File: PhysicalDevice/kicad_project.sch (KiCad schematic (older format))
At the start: 22 parts, among them J1 Conn_01x06, SW1 SW_Push, SW2 SW_Push, SW3 SW_Push, U1 MAX7219CWGT, U3 AMS1117-3.3

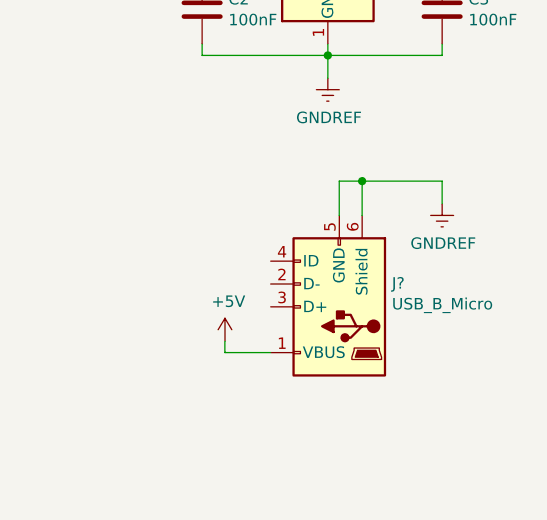
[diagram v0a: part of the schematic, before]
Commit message: Board fully routed. Gerber file generated.
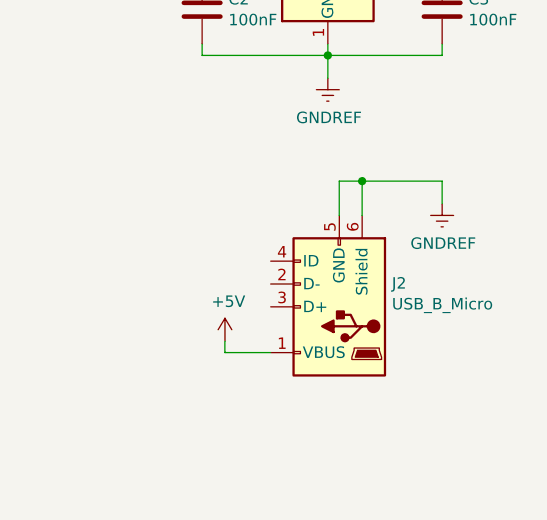
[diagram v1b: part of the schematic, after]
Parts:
- gave numbers to parts that had none: 1
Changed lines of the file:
@@
 BUT_OFFSET
 $Comp
-L Connector:USB_B_Micro J?
+L Connector:USB_B_Micro J2
 U 1 1 5D204B92
 P 9550 5350
-F 0 "J?" H 9320 5247 50  0000 R CNN
+F 0 "J2" H 9320 5247 50  0000 R CNN
 F 1 "USB_B_Micro" H 9320 5338 50  0000 R CNN
 F 2 "Connector_USB:USB_Micro-B_Molex-105017-0001" H 9700 5300 50  0001 C CNN
@@
 $EndComp
 $Comp
-L power:GNDREF #PWR?
+L power:GNDREF #PWR0117
 U 1 1 5D2071A6
 P 10000 4900
-F 0 "#PWR?" H 10000 4650 50  0001 C CNN
+F 0 "#PWR0117" H 10000 4650 50  0001 C CNN
 F 1 "GNDREF" H 10005 4727 50  0000 C CNN
 F 2 "" H 10000 4900 50  0001 C CNN
@@
 	9650 4800 10000 4800
 $Comp
-L power:+5V #PWR?
+L power:+5V #PWR0118
 U 1 1 5D20C16A
 P 9050 5500
-F 0 "#PWR?" H 9050 5350 50  0001 C CNN
+F 0 "#PWR0118" H 9050 5350 50  0001 C CNN
 F 1 "+5V" H 9065 5673 50  0000 C CNN
 F 2 "" H 9050 5500 50  0001 C CNN

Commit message: added leds and rerouted some bits to be more tidy
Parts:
- added CONN1, WPS1: LED, LED_SMD:LED_0805_2012Metric_Pad1.15x1.40mm_HandSolder, symbol Device:LED
- added R8: 220R, Resistor_SMD:R_0805_2012Metric_Pad1.15x1.40mm_HandSolder, symbol Device:R_Small
- added R9: 2204, Resistor_SMD:R_0805_2012Metric_Pad1.15x1.40mm_HandSolder, symbol Device:R_Small
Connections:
- net GNDREF: now also CONN1.1 (K), WPS1.1 (K)
- net LED_CONN: now reaches ESP12E1.17 (GPIO2)
- net LED_CONN: now also R9.2
- net LED_WPS: now reaches ESP12E1.4 (GPIO16)
- net LED_WPS: now also R8.2
- new net: R8.1, WPS1.2 (A)
- new net: CONN1.2 (A), R9.1
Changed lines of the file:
@@
 Wire Wire Line
 	9050 5550 9050 5500
+$Comp
+L Device:R_Small R8
+U 1 1 5D140AC3
+P 6100 5500
+F 0 "R8" H 6159 5546 50  0000 L CNN
+F 1 "220R" H 6159 5455 50  0000 L CNN
+F 2 "Resistor_SMD:R_0805_2012Metric_Pad1.15x1.40mm_HandSolder" H 6100 5500 50  0001 C CNN
+F 3 "~" H 6100 5500 50  0001 C CNN
+	1    6100 5500
+	0    1    1    0
+$EndComp
+$Comp
+L Device:R_Small R9
+U 1 1 5D142792
+P 6100 5900
+F 0 "R9" H 6159 5946 50  0000 L CNN
+F 1 "2204" H 6159 5855 50  0000 L CNN
+F 2 "Resistor_SMD:R_0805_2012Metric_Pad1.15x1.40mm_HandSolder" H 6100 5900 50  0001 C CNN
+F 3 "~" H 6100 5900 50  0001 C CNN
+	1    6100 5900
+	0    1    1    0
+$EndComp
+Wire Wire Line
+	6650 5500 6850 5500
+Wire Wire Line
+	6850 5500 6850 5900
+Wire Wire Line
+	6850 5900 6650 5900
+Wire Wire Line
+	6850 5900 6850 6000
+Connection ~ 6850 5900
+$Comp
+L power:GNDREF #PWR0119
+U 1 1 5D14BF49
+P 6850 6000
+F 0 "#PWR0119" H 6850 5750 50  0001 C CNN
+F 1 "GNDREF" H 6855 5827 50  0000 C CNN
+F 2 "" H 6850 6000 50  0001 C CNN
+F 3 "" H 6850 6000 50  0001 C CNN
+	1    6850 6000
+	1    0    0    -1
+$EndComp
+Text Label 7250 1800 0    50   ~ 0
+LED_CONN
+Text Label 7250 2600 3    50   ~ 0
+LED_WPS
+Text Label 6000 5900 2    50   ~ 0
+LED_CONN
+Text Label 6000 5500 2    50   ~ 0
+LED_WPS
+$Comp
+L Device:LED CONN1
+U 1 1 5D139E9D
+P 6500 5900
+F 0 "CONN1" H 6493 5645 50  0000 C CNN
+F 1 "LED" H 6493 5736 50  0000 C CNN
+F 2 "LED_SMD:LED_0805_2012Metric_Pad1.15x1.40mm_HandSolder" H 6500 5900 50  0001 C CNN
+F 3 "~" H 6500 5900 50  0001 C CNN
+	1    6500 5900
+	-1   0    0    1
+$EndComp
+$Comp
+L Device:LED WPS1
+U 1 1 5D138DE4
+P 6500 5500
+F 0 "WPS1" H 6493 5245 50  0000 C CNN
+F 1 "LED" H 6493 5336 50  0000 C CNN
+F 2 "LED_SMD:LED_0805_2012Metric_Pad1.15x1.40mm_HandSolder" H 6500 5500 50  0001 C CNN
+F 3 "~" H 6500 5500 50  0001 C CNN
+	1    6500 5500
+	-1   0    0    1
+$EndComp
+Wire Wire Line
+	6200 5500 6350 5500
+Wire Wire Line
+	6350 5900 6200 5900
 $EndSCHEMATC

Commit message: pre track witdh change
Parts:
- added SW4: SW_Push, KicadLibrary:DTS-3, symbol Switch:SW_Push
- SW1, SW2, SW3: footprint Button_Switch_THT:SW_PUSH_6mm -> KicadLibrary:DTS-3
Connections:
- net DIG_4 is gone; now on net GNDREF: U1.3 (DIG_4)
- net DIG_5 is gone; now on net GNDREF: U1.10 (DIG_5)
- net DIG_7 is gone; now on net GNDREF: U1.8 (DIG_7)
- net DIG_1: no longer DIG1.8 (CC)
- net DIG_2: no longer DIG2.3 (CC)
- net DIG_3: no longer DIG3.3 (CC)
- net GNDREF: now also DIG0.8 (CC), U1.2 (DIG_0), SW4.2
- net BUT_RST: now reaches ESP12E1.1 (~RST), J1.2 (Pin_2), R5.2
- net BUT_RST: now also SW4.1
- removed net DIG_0: DIG0.3 (CC), DIG0.8 (CC), U1.2 (DIG_0)
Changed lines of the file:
@@
 	900  1650 1450 1650
 Wire Wire Line
-	900  2150 1450 2150
+	900  2150 1150 2150
 Text Label 1450 1450 2    50   ~ 0
 DIG_0
@@
 Text Label 1600 4150 2    50   ~ 0
 SEG_DP
-Text Label 2200 4050 0    50   ~ 0
-DIG_0
 Text Label 2200 4150 0    50   ~ 0
 DIG_0
@@
 SEG_DP
 Text Label 3800 4050 0    50   ~ 0
-DIG_1
-Text Label 3800 4150 0    50   ~ 0
 DIG_1
 Text Label 1700 5700 2    50   ~ 0
@@
 Text Label 3200 6100 2    50   ~ 0
 SEG_DP
-Text Label 2300 6000 0    50   ~ 0
-DIG_2
 Text Label 2300 6100 0    50   ~ 0
 DIG_2
-Text Label 3800 6000 0    50   ~ 0
-DIG_3
 Text Label 3800 6100 0    50   ~ 0
 DIG_3
@@
 F 0 "SW2" H 6200 4435 50  0000 C CNN
 F 1 "SW_Push" H 6200 4344 50  0000 C CNN
-F 2 "Button_Switch_THT:SW_PUSH_6mm" H 6200 4350 50  0001 C CNN
+F 2 "KicadLibrary:DTS-3" H 6200 4350 50  0001 C CNN
 F 3 "" H 6200 4350 50  0001 C CNN
 	1    6200 4150
@@
 F 0 "SW3" H 6200 4835 50  0000 C CNN
 F 1 "SW_Push" H 6200 4744 50  0000 C CNN
-F 2 "Button_Switch_THT:SW_PUSH_6mm" H 6200 4750 50  0001 C CNN
+F 2 "KicadLibrary:DTS-3" H 6200 4750 50  0001 C CNN
 F 3 "" H 6200 4750 50  0001 C CNN
 	1    6200 4550
@@
 L power:GNDREF #PWR0116
 U 1 1 5D1B2226
-P 6600 4700
-F 0 "#PWR0116" H 6600 4450 50  0001 C CNN
-F 1 "GNDREF" H 6605 4527 50  0000 C CNN
-F 2 "" H 6600 4700 50  0001 C CNN
-F 3 "" H 6600 4700 50  0001 C CNN
-	1    6600 4700
-	1    0    0    -1
-$EndComp
-Wire Wire Line
-	6600 4700 6600 4550
+P 6600 5000
+F 0 "#PWR0116" H 6600 4750 50  0001 C CNN
+F 1 "GNDREF" H 6605 4827 50  0000 C CNN
+F 2 "" H 6600 5000 50  0001 C CNN
+F 3 "" H 6600 5000 50  0001 C CNN
+	1    6600 5000
+	1    0    0    -1
+$EndComp
 Wire Wire Line
 	6600 4550 6400 4550
@@
 F 0 "SW1" H 6200 3985 50  0000 C CNN
 F 1 "SW_Push" H 6200 3894 50  0000 C CNN
-F 2 "Button_Switch_THT:SW_PUSH_6mm" H 6200 3900 50  0001 C CNN
+F 2 "KicadLibrary:DTS-3" H 6200 3900 50  0001 C CNN
 F 3 "" H 6200 3900 50  0001 C CNN
 	1    6200 3700
@@
 Wire Wire Line
 	6350 5900 6200 5900
+Wire Wire Line
+	6600 4550 6600 4900
+$Comp
+L Switch:SW_Push SW4
+U 1 1 5D145BE2
+P 6200 4900
+F 0 "SW4" H 6200 5185 50  0000 C CNN
+F 1 "SW_Push" H 6200 5094 50  0000 C CNN
+F 2 "KicadLibrary:DTS-3" H 6200 5100 50  0001 C CNN
+F 3 "" H 6200 5100 50  0001 C CNN
+	1    6200 4900
+	1    0    0    -1
+$EndComp
+Wire Wire Line
+	6400 4900 6600 4900
+Connection ~ 6600 4900
+Wire Wire Line
+	6600 4900 6600 5000
+Text Label 6000 4900 2    50   ~ 0
+BUT_RST
+Text Label 5900 1100 0    50   ~ 0
+BUT_RST
+Wire Wire Line
+	1450 1450 900  1450
+Wire Wire Line
+	900  1450 900  1550
+Connection ~ 900  1650
+Wire Wire Line
+	900  1550 1450 1550
+Connection ~ 900  1550
+Wire Wire Line
+	900  1550 900  1650
+Wire Wire Line
+	1450 2050 900  2050
+Wire Wire Line
+	900  2050 900  2150
+Connection ~ 900  2150
+Wire Wire Line
+	1450 2250 1150 2250
+Wire Wire Line
+	1150 2250 1150 2150
+Connection ~ 1150 2150
+Wire Wire Line
+	1150 2150 1450 2150
 $EndSCHEMATC

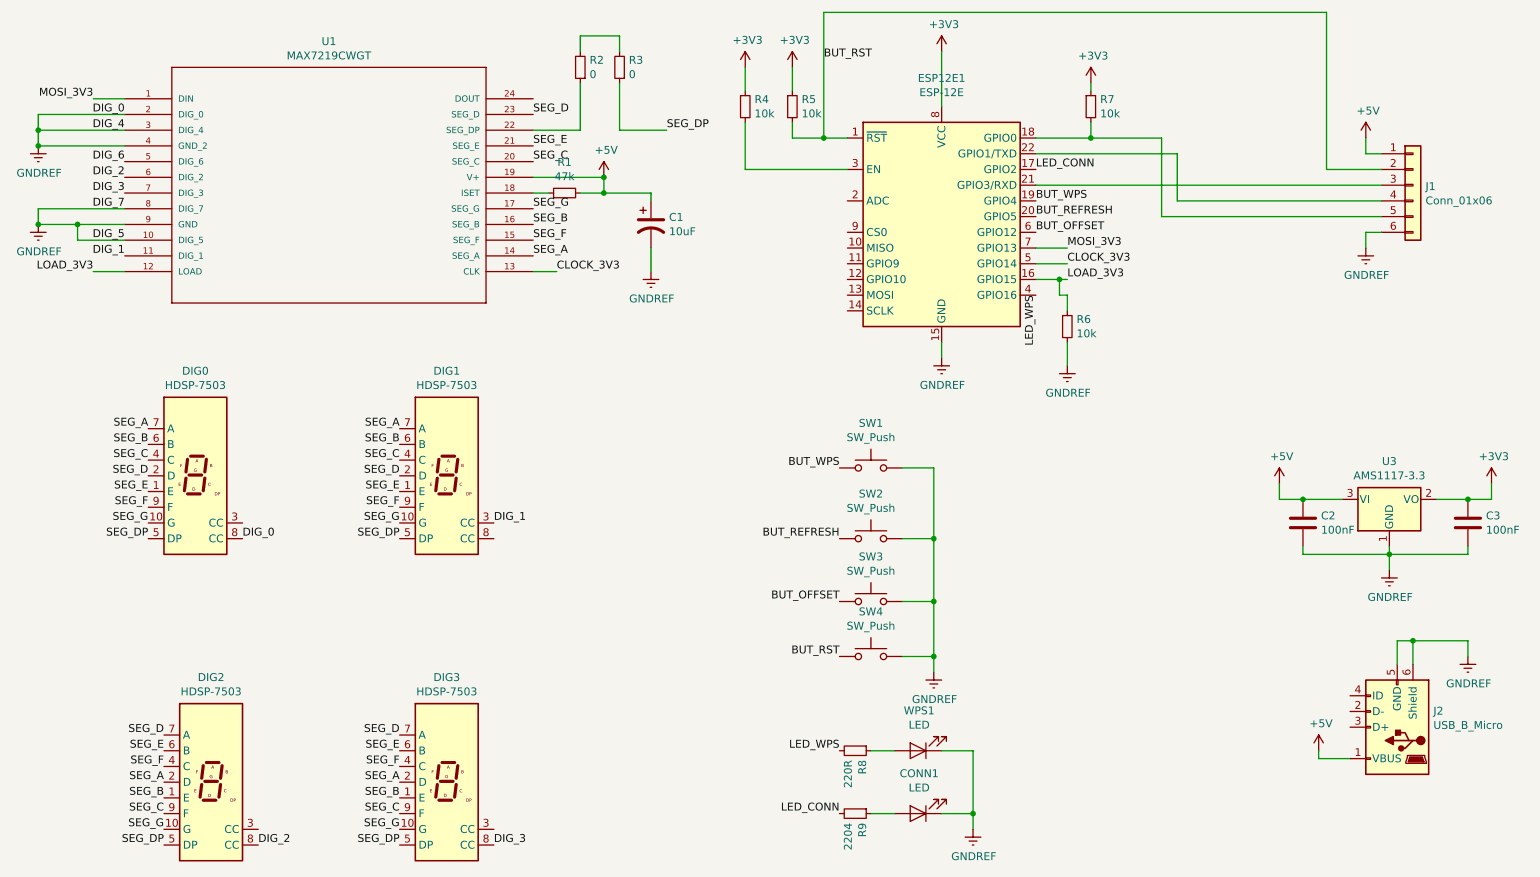
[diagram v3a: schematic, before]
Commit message: changed min routing size from 0.25mm(~9.8mil) to 0.35(~13.4mil)
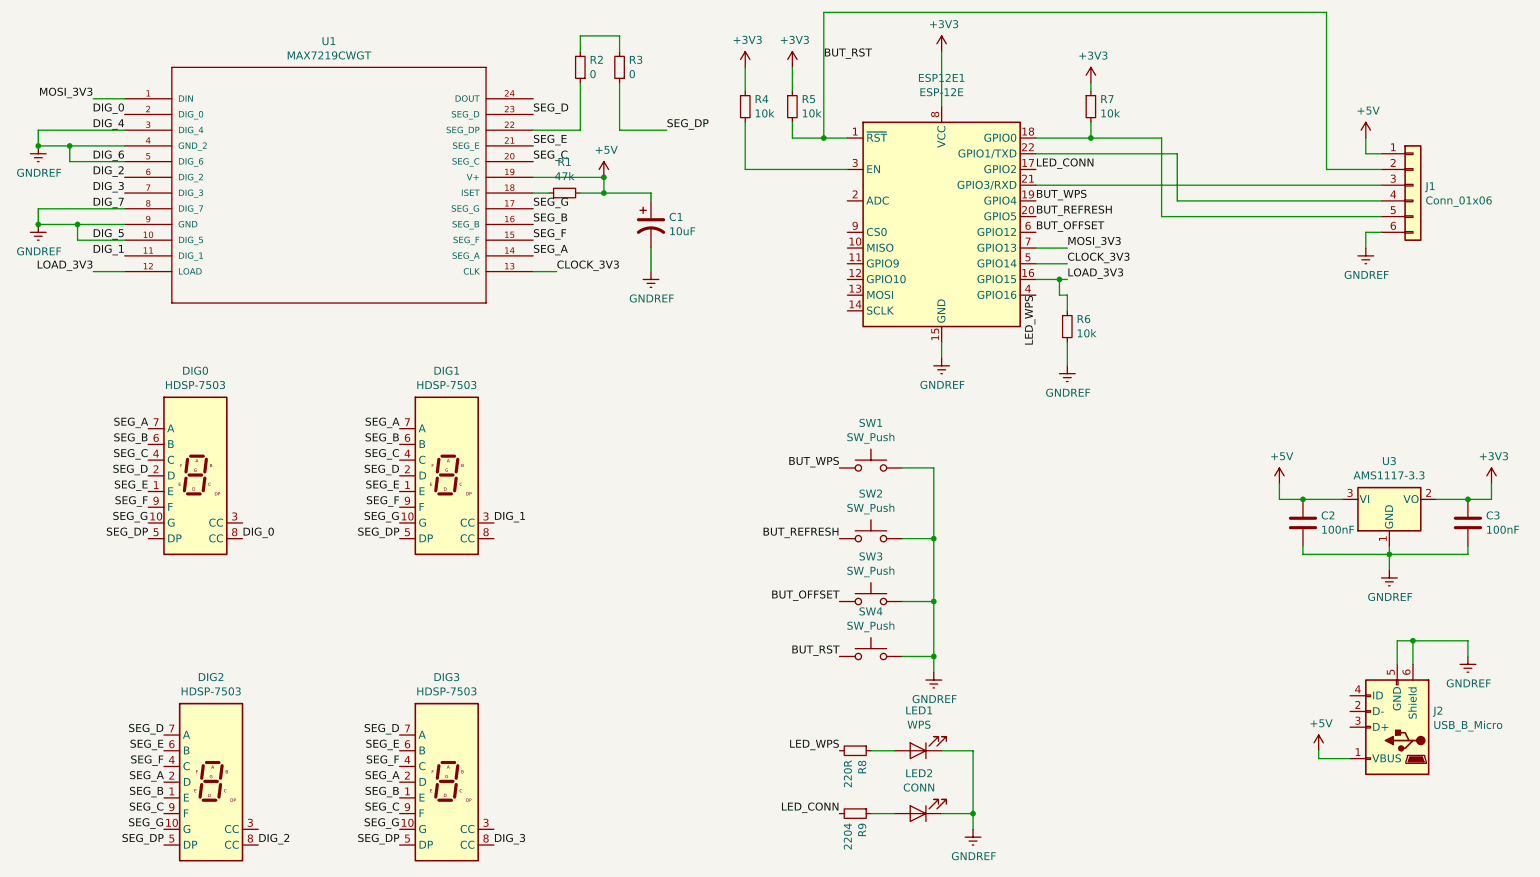
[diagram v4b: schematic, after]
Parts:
- LED1: renamed from WPS1; value LED -> WPS
- LED2: renamed from CONN1; value LED -> CONN
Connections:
- net DIG_6 is gone; now on net GNDREF: U1.5 (DIG_6)
- net GNDREF: no longer DIG0.8 (CC), U1.2 (DIG_0)
- new net DIG_0: DIG0.8 (CC), U1.2 (DIG_0)
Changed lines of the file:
@@
 $EndComp
 Wire Wire Line
-	900  1650 1450 1650
+	900  1650 1100 1650
 Wire Wire Line
 	900  2150 1150 2150
@@
 LED_WPS
 $Comp
-L Device:LED CONN1
+L Device:LED LED2
 U 1 1 5D139E9D
 P 6500 5900
-F 0 "CONN1" H 6493 5645 50  0000 C CNN
-F 1 "LED" H 6493 5736 50  0000 C CNN
+F 0 "LED2" H 6493 5645 50  0000 C CNN
+F 1 "CONN" H 6493 5736 50  0000 C CNN
 F 2 "LED_SMD:LED_0805_2012Metric_Pad1.15x1.40mm_HandSolder" H 6500 5900 50  0001 C CNN
 F 3 "~" H 6500 5900 50  0001 C CNN
@@
 $EndComp
 $Comp
-L Device:LED WPS1
+L Device:LED LED1
 U 1 1 5D138DE4
 P 6500 5500
-F 0 "WPS1" H 6493 5245 50  0000 C CNN
-F 1 "LED" H 6493 5336 50  0000 C CNN
+F 0 "LED1" H 6493 5245 50  0000 C CNN
+F 1 "WPS" H 6493 5336 50  0000 C CNN
 F 2 "LED_SMD:LED_0805_2012Metric_Pad1.15x1.40mm_HandSolder" H 6500 5500 50  0001 C CNN
 F 3 "~" H 6500 5500 50  0001 C CNN
@@
 Text Label 5900 1100 0    50   ~ 0
 BUT_RST
-Wire Wire Line
-	1450 1450 900  1450
-Wire Wire Line
-	900  1450 900  1550
 Connection ~ 900  1650
 Wire Wire Line
 	900  1550 1450 1550
-Connection ~ 900  1550
 Wire Wire Line
 	900  1550 900  1650
@@
 Wire Wire Line
 	1150 2150 1450 2150
+Wire Wire Line
+	1450 1750 1100 1750
+Wire Wire Line
+	1100 1750 1100 1650
+Connection ~ 1100 1650
+Wire Wire Line
+	1100 1650 1450 1650
 $EndSCHEMATC
